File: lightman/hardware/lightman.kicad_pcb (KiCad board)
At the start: 2 copper layers, 139 x 80 mm, 39 parts, among them J1 DE15_Socket_HighDensity_Mount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, J2 Mini-DIN-6, J4 DE9_Pins, J5 Barrel_Jack_Switch, SW23 POWER, U1 MAX3232, U2 L7805, U3 MAX3232

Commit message: lightman pcb
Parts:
- added C13: 100n, IMNOTWOPR:C_Rect_P200mil, F.Cu at (71.8, 93.1)
- added C14: 100n, IMNOTWOPR:C_Rect_P200mil, F.Cu at (71.8, 100.7)
- added C15: 100n, IMNOTWOPR:C_Rect_P200mil, F.Cu at (69.3, 105.8)
- added C16: 100n, IMNOTWOPR:C_Rect_P200mil, F.Cu at (69.3, 95.6)
- added C17: 100n, IMNOTWOPR:C_Rect_P200mil, F.Cu at (80.7, 86.7)
- added F1: Polyfuse, Fuse:Fuse_Bourns_MF-RG700, F.Cu at (94.7, 60.0)
- added U5: MAX3232, IMNOTWOPR:DIP-16N, F.Cu at (79.5, 99.4)
- D3: footprint LED_THT:LED_D5.0mm -> LED_THT:LED_D5.0mm_Horizontal_O1.27mm_Z3.0mm
- R21: value 470 -> 1k
- U4: value ~ -> LEVEL SHIFTER
- moved A1 110.3 mm to (90.9, 88.0), turned to 0 degrees
- moved U4 96.5 mm to (76.9, 128.7), turned to 90 degrees
- moved J1 84.3 mm to (121.1, 148.1), turned to 0 degrees
- moved R4 67.2 mm to (130.3, 135.0), turned to -90 degrees
- moved J4 66.7 mm to (122.3, 54.4)
- moved U1 61.2 mm to (122.6, 62.6)
- moved R5 60.6 mm to (125.3, 135.0), turned to -90 degrees
- moved U3 60.6 mm to (122.6, 80.4)
- moved J2 55.8 mm to (88.1, 152.7)
- moved R6 54.2 mm to (120.3, 135.0), turned to -90 degrees
- moved R7 47.9 mm to (115.3, 135.0), turned to -90 degrees
- moved R8 45.8 mm to (130.1, 118.5), turned to -90 degrees
- moved R21 42.8 mm to (74.4, 151.5), turned to -90 degrees
- moved D3 41.6 mm to (68.2, 157.0)
- moved R9 40.0 mm to (125.3, 118.5), turned to -90 degrees
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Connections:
- A1 pad 10: /KEY_DATA_LO -> /PICO_RI
- A1 pad 11: unconnected-(A1-GPIO8-Pad11) -> /KEY_CLOCK_LO
- A1 pad 12: unconnected-(A1-GPIO9-Pad12) -> /KEY_DATA_LO
- A1 pad 9: /KEY_CLOCK_LO -> /PICO_DCD
- J4 pad 9: unconnected-(J4-Pad9) -> /RI
- J5 pad 1: Net-(D2-A) -> Net-(F1-Pad1)
- R21 pad 1: +9V -> +5V
- U3 pad 12: unconnected-(U3-R1OUT-Pad12) -> /PICO_DSR
- U3 pad 13: /DCD -> /DSR
- U3 pad 7: /RTR -> unconnected-(U3-T2OUT-Pad7)
- U3 pad 8: /DSR -> unconnected-(U3-R2IN-Pad8)
- U3 pad 9: /PICO_DSR -> unconnected-(U3-R2OUT-Pad9)
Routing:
- net GND: track 0.00 -> 457.9 mm
- net +5V: track 0.00 -> 122.8 mm
- net +3V3: track 0.00 -> 121.2 mm
- net /RI: track 0.00 -> 78.2 mm
- net /DCD: track 0.00 -> 70.0 mm
- net /BLUE: track 0.00 -> 56.1 mm
- net Net-(A1-GPIO20): track 0.00 -> 48.0 mm
- net +9V: track 0.00 -> 41.9 mm
- net /GREEN: track 0.00 -> 38.7 mm
- net /PICO_DSR: track 0.00 -> 38.6 mm
- net /PICO_DTR: track 0.00 -> 37.3 mm
- net /PICO_RTS: track 0.00 -> 36.0 mm
- net /PICO_CTS: track 0.00 -> 34.8 mm
- net /CTS: track 0.00 -> 33.0 mm
- net Net-(A1-GPIO19): track 0.00 -> 31.6 mm
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- added copper zone on B.Cu, net GND
- added copper zone on F.Cu, net GND
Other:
- board size 139 x 80 mm -> 74 x 119 mm
- board text added: "${COMPANY}"

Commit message: lightman pcb
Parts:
- removed R12, R13, R14, R15: 1k, IMNOTWOPR:R_Axial_DIN0207_P400mil
- C1: renamed from C31; footprint Desval27:C_Disc_D5.0mm_W2.5mm_P200mil -> IMNOTWOPR:C_Rect_P200mil
- C4: renamed from C30; footprint Desval27:C_Disc_D5.0mm_W2.5mm_P200mil -> IMNOTWOPR:C_Rect_P200mil
- R1: renamed from R21; footprint Desval27:R_Axial_DIN0207_400mil -> IMNOTWOPR:R_Axial_DIN0207_P400mil
- R2: renamed from R4; value 1k -> 470R
- R4: renamed from R6; value 1k -> 2k2
- R5: renamed from R7; value 1k -> 470R
- R7: renamed from R9; value 1k -> 2k2
- R8: renamed from R10; value 1k -> 390R
- moved C13 59.8 mm to (129.0, 109.6), turned to 0 degrees
- moved C10 52.5 mm to (123.9, 107.1), turned to 0 degrees
- moved C16 51.5 mm to (118.8, 109.6), turned to 0 degrees
- moved C7 46.6 mm to (116.3, 107.1), turned to 0 degrees
- moved U5 43.2 mm to (122.6, 99.5), turned to 90 degrees
- moved C19 31.4 mm to (109.9, 98.2), turned to -90 degrees
- moved R6 10.7 mm to (122.6, 126.1), turned to 0 degrees
- moved R5 8.96 mm to (122.6, 129.9), turned to 0 degrees
- moved R2 8.13 mm to (125.2, 141.4), turned to 0 degrees
- moved A1 6.35 mm to (87.1, 93.1)
- moved R9 6.16 mm to (120.1, 114.7), turned to 0 degrees
- moved R4 5.08 mm to (125.2, 133.7), turned to 0 degrees
- moved R7 4.62 mm to (122.6, 122.3), turned to 0 degrees
- moved U1 2.84 mm to (75.7, 131.2)
- moved R3 2.54 mm to (125.2, 137.6), turned to 0 degrees
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- renumbered C14 to C10, C6 to C11, C10 to C12, C15 to C13, C5 to C14, C11 to C15, C7 to C17, C12 to C18, C17 to C19, C1 to C2, C2 to C3, C3 to C5, C8 to C6, C13 to C7, C4 to C8, D2 to D1, D3 to D2, J5 to J1, J1 to J3, R5 to R3, R8 to R6, R11 to R9, SW23 to SW1, U4 to U1, U1 to U3, U3 to U4
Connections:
- A1 pad 1: /PICO_TXD -> /PICO_RXD
- A1 pad 17: unconnected-(A1-GPIO13-Pad17) -> /HSYNC
- A1 pad 19: unconnected-(A1-GPIO14-Pad19) -> /VSYNC
- A1 pad 2: /PICO_RXD -> /PICO_TXD
- A1 pad 20: unconnected-(A1-GPIO15-Pad20) -> /R0
- A1 pad 21: /HSYNC -> /R1
- A1 pad 22: /VSYNC -> /R2
- A1 pad 24: Net-(A1-GPIO18) -> /G0
- A1 pad 25: Net-(A1-GPIO19) -> /G1
- A1 pad 26: Net-(A1-GPIO20) -> /G2
- A1 pad 27: unconnected-(A1-GPIO21-Pad27) -> /B0
- A1 pad 29: unconnected-(A1-GPIO22-Pad29) -> /B1
- A1 pad 4: /PICO_CTS -> /PICO_RTS
- A1 pad 5: /PICO_RTS -> /PICO_CTS
- A1 pad 6: /PICO_DTR -> /PICO_DSR
- A1 pad 7: /PICO_DSR -> /PICO_DTR
- R2 pad 1: Net-(A1-GPIO18) -> /R0
- R3 pad 1: Net-(A1-GPIO18) -> /R1
- R4 pad 1: Net-(A1-GPIO18) -> /R2
- R5 pad 1: Net-(A1-GPIO18) -> /G0
- R5 pad 2: /RED -> /GREEN
- R6 pad 1: Net-(A1-GPIO19) -> /G1
- R7 pad 1: Net-(A1-GPIO19) -> /G2
- R8 pad 1: Net-(A1-GPIO19) -> /B0
- R8 pad 2: /GREEN -> /BLUE
- R9 pad 1: Net-(A1-GPIO19) -> /B1
- R9 pad 2: /GREEN -> /BLUE
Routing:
- net GND: track 457.9 -> 191.5 mm
- net /PICO_RI: track 8.74 -> 64.8 mm
- net /PICO_CTS: track 34.8 -> 88.9 mm
- net /R0: track 0.00 -> 49.9 mm
- net Net-(A1-GPIO20): track 48.0 -> 0.00 mm
- net /PICO_RTS: track 36.0 -> 83.8 mm
- net /PICO_TXD: track 29.7 -> 76.2 mm
- net /PICO_DCD: track 12.4 -> 56.4 mm
- net /PICO_RXD: track 31.0 -> 71.1 mm
- net /DSR: track 0.00 -> 38.9 mm
- net /PICO_DTR: track 37.3 -> 70.5 mm
- net Net-(A1-GPIO19): track 31.6 -> 0.00 mm
- net /PICO_DSR: track 38.6 -> 65.4 mm
- net /DCD: track 70.0 -> 46.1 mm, vias 0 -> 1
- net Net-(A1-GPIO18): track 21.6 -> 0.00 mm
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
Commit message: routing-first-stage
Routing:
- net +3V3: track 114.6 -> 0.00 mm, vias 1 -> 0
- net +5V: track 129.3 -> 16.6 mm
- net GND: track 191.5 -> 94.8 mm, vias 0 -> 8
- net /PICO_CTS: track 88.9 -> 0.00 mm
- net /PICO_RTS: track 83.8 -> 0.00 mm
- net /PICO_TXD: track 76.2 -> 0.00 mm
- net /PICO_RXD: track 71.1 -> 0.00 mm
- net /PICO_DTR: track 70.5 -> 0.00 mm
- net /PICO_DSR: track 65.4 -> 0.00 mm
- net /PICO_RI: track 64.8 -> 0.00 mm
- net /RI: track 60.2 -> 0.00 mm
- net /PICO_DCD: track 56.4 -> 0.00 mm
- net /R0: track 49.9 -> 0.00 mm
- net /HSYNC: track 48.4 -> 0.00 mm
- net /DCD: track 46.1 -> 0.00 mm, vias 1 -> 0
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
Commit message: numerous updates; documentation, ferruous, lightman, etc.
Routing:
- net GND: track 94.8 -> 536.3 mm
- net +3V3: track 0.00 -> 112.1 mm
- net +5V: track 16.6 -> 119.3 mm
- net /RI: track 0.00 -> 70.8 mm
- net /HSYNC: track 0.00 -> 48.6 mm
- net /VSYNC: track 0.00 -> 38.4 mm
- net /BLUE: track 0.00 -> 37.5 mm
- net /R0: track 0.00 -> 33.3 mm
- net /GREEN: track 0.00 -> 30.0 mm
- net /RTS: track 0.00 -> 29.4 mm
- net /CTS: track 0.00 -> 24.6 mm
- net /RED: track 0.00 -> 22.8 mm
- net /KEY_DATA_HI: track 0.00 -> 18.5 mm
- net /KEY_CLOCK_HI: track 0.00 -> 18.0 mm
- net /R2: track 0.00 -> 16.1 mm
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
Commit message: tracework for lightman
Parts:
- moved C1 2.54 mm to (70.6, 71.5)
- moved C3 2.54 mm to (89.6, 67.7)
- moved U2 2.54 mm to (78.2, 81.7)
- moved C2 2.54 mm to (69.3, 65.2)
- moved D1 2.54 mm to (68.0, 57.5)
- moved F1 2.54 mm to (94.7, 62.5)
- moved J1 2.54 mm to (91.9, 56.9)
- moved C4 2.54 mm to (90.9, 74.0)
- moved SW1 1.27 mm to (77.7, 49.3)
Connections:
- A1 pad 1: /PICO_RXD -> /PICO_TXD
- A1 pad 2: /PICO_TXD -> /PICO_RXD
- A1 pad 4: /PICO_RTS -> /PICO_CTS
- A1 pad 5: /PICO_CTS -> /PICO_RTS
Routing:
- net /PICO_CTS: track 0.00 -> 77.2 mm
- net /PICO_RTS: track 0.00 -> 73.0 mm
- net /PICO_TXD: track 0.00 -> 64.6 mm
- net /PICO_RXD: track 0.00 -> 61.4 mm
- net /DCD: track 0.00 -> 56.5 mm
- net /PICO_DTR: track 0.00 -> 55.6 mm
- net /PICO_RI: track 0.00 -> 52.9 mm
- net /PICO_DSR: track 0.00 -> 51.6 mm
- net /DSR: track 0.00 -> 44.7 mm
- net /PICO_DCD: track 0.00 -> 44.2 mm
- net /DTR: track 0.00 -> 24.8 mm
- net GND: track 536.3 -> 557.1 mm, vias 8 -> 0
- net /CTS: track 24.6 -> 37.8 mm
- net /RTS: track 29.4 -> 18.8 mm
- net +5V: track 119.3 -> 114.6 mm
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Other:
- board text added: "${COMMENT3}"
- board text added: "${COMPANY} - ${COMMENT1} ${TITLE} | ${COMMENT4} | ${COMMENT2} REVISION ${REVISION} ${CURRENT_DATE}"
- board text removed: "${COMPANY}"

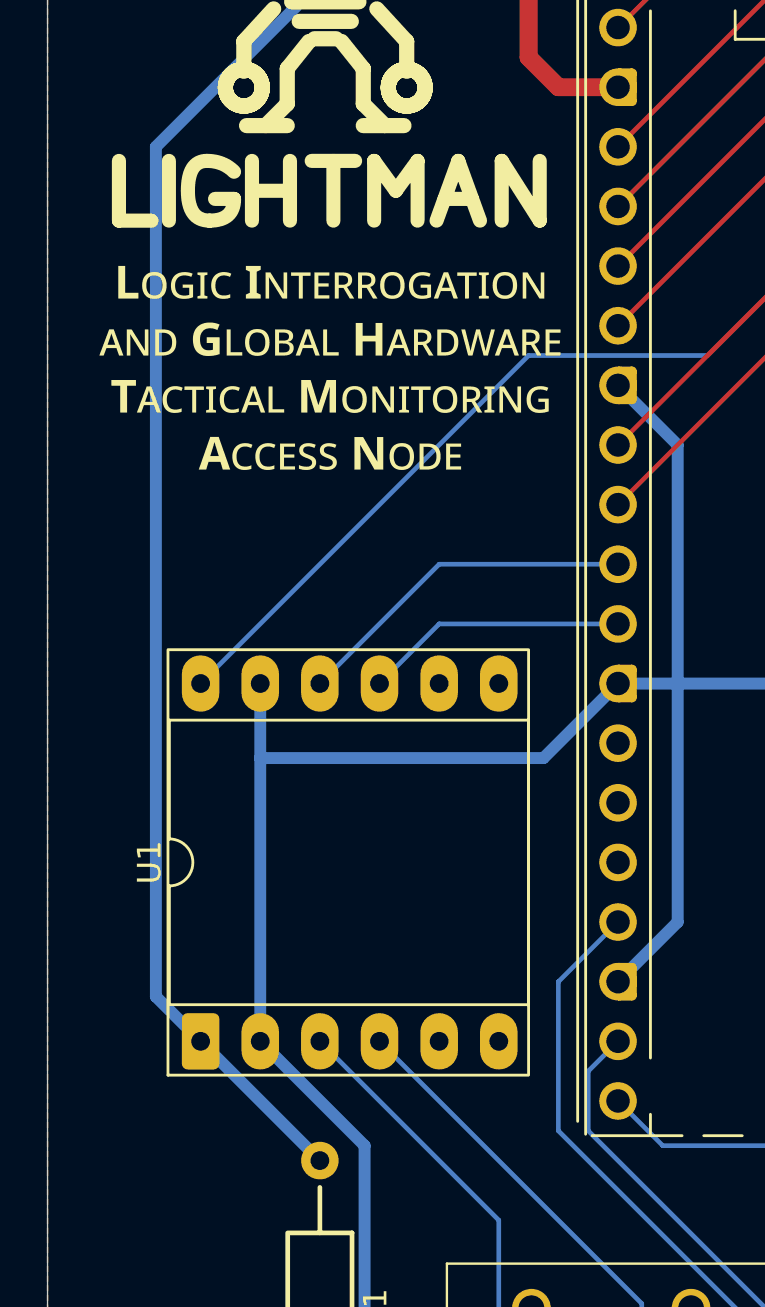
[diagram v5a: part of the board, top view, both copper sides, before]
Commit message: fixed level shifter footprint width
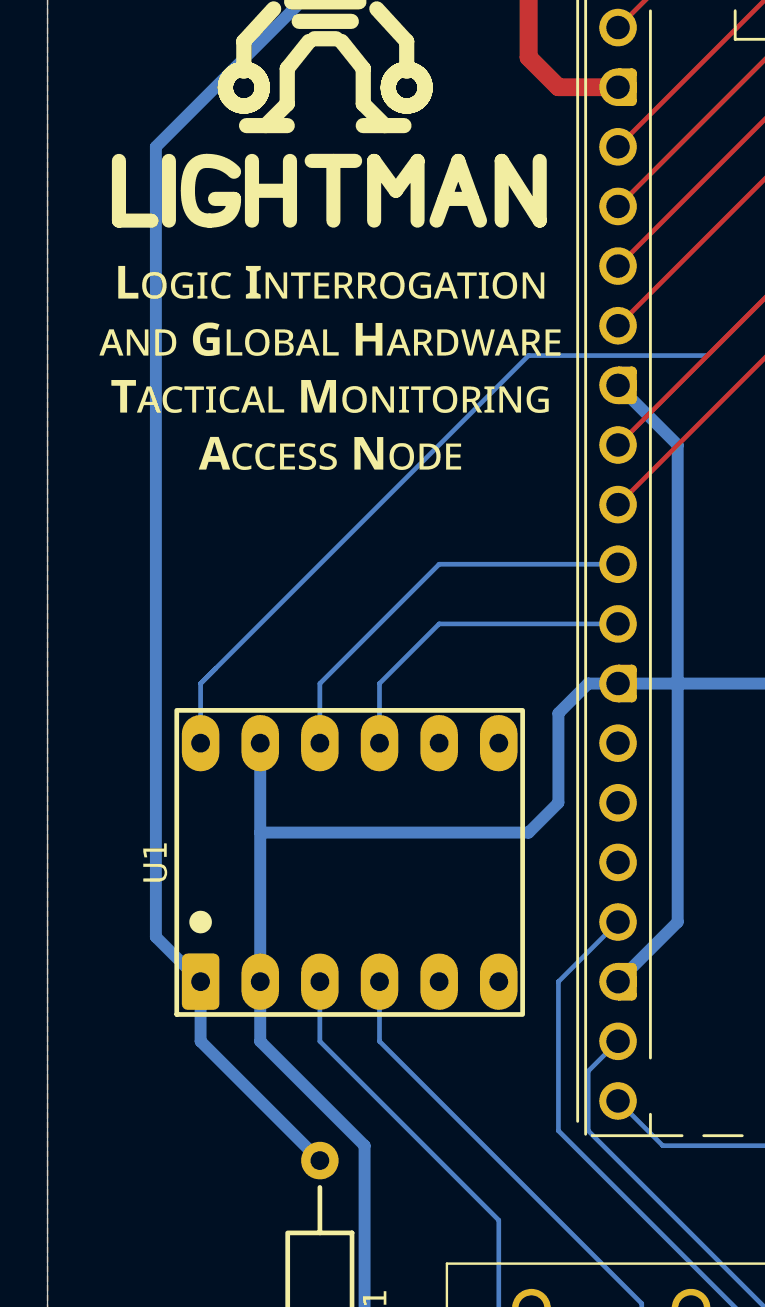
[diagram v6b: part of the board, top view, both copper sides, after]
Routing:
- net +3V3: track 110.2 -> 113.6 mm
- net /KEY_DATA_LO: track 11.2 -> 13.8 mm
- net /KEY_CLOCK_LO: track 14.8 -> 17.3 mm
- net /KEY_DATA_HI: track 18.5 -> 21.0 mm
- net /KEY_CLOCK_HI: track 17.6 -> 20.1 mm
- net GND: track 557.1 -> 558.1 mm

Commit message: lightman cleanup; more work pending
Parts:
- C2: footprint Capacitor_THT:CP_Radial_D6.3mm_P2.50mm -> Capacitor_THT:CP_Radial_D10.0mm_P5.00mm
- C3: footprint Capacitor_THT:CP_Radial_D5.0mm_P2.50mm -> Capacitor_THT:CP_Radial_D10.0mm_P5.00mm
- moved C3 21.9 mm to (72.7, 81.7)
- moved C4 21.9 mm to (75.2, 89.3)
- moved U2 7.41 mm to (84.5, 85.5)
- moved C1 5.51 mm to (75.2, 74.5)
- moved C2 3.90 mm to (72.7, 67.1)
- moved F1 2.66 mm to (92.2, 63.3)
- moved R1 2.57 mm to (76.9, 150.7)
- turned U1 to -90 degrees
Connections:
- U1 pad 1: +5V -> /KEY_DATA_LO
- U1 pad 10: /KEY_CLOCK_LO -> +5V
- U1 pad 11: GND -> /KEY_CLOCK_HI
- U1 pad 12: +3V3 -> /KEY_DATA_HI
- U1 pad 2: GND -> /KEY_CLOCK_LO
- U1 pad 3: /KEY_CLOCK_HI -> +3V3
- U1 pad 4: /KEY_DATA_HI -> GND
- U1 pad 9: /KEY_DATA_LO -> GND
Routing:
- net GND: track 558.1 -> 493.6 mm
- net +5V: track 114.6 -> 87.2 mm
- net +9V: track 43.6 -> 30.3 mm
- net Net-(D1-A): track 7.93 -> 0.00 mm
- net Net-(F1-Pad1): track 6.84 -> 0.00 mm
- net +3V3: track 113.6 -> 109.6 mm
- net /KEY_DATA_LO: track 13.8 -> 10.2 mm
- net Net-(D2-A): track 3.19 -> 6.14 mm
- net /KEY_DATA_HI: track 21.0 -> 18.9 mm
- net /KEY_CLOCK_HI: track 20.1 -> 18.0 mm
- net /KEY_CLOCK_LO: track 17.3 -> 15.2 mm
- net unconnected-(U1-LV3-Pad5): track 0.00 -> 0.63 mm

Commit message: lightman pcb gerbers
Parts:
- J4: footprint Connector_Dsub:DSUB-9_Pins_Horizontal_P2.77x2.54mm_EdgePinOffset9.40mm -> IMNOTWOPR:D-Sub 9 CNR Series
- moved J4 5.66 mm to (117.2, 52.0), turned to 0 degrees
- moved F1 0.24 mm to (91.9, 63.3)
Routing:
- net GND: track 493.6 -> 529.5 mm
- net +5V: track 87.2 -> 119.9 mm
- net +9V: track 30.3 -> 50.3 mm
- net Net-(D1-A): track 0.00 -> 6.92 mm
- net Net-(F1-Pad1): track 0.00 -> 6.38 mm
- net /DSR: track 44.7 -> 49.2 mm
- net /RTS: track 18.8 -> 20.7 mm
- net /TXD: track 5.23 -> 6.17 mm
- net /DTR: track 24.8 -> 25.6 mm
- net /RXD: track 5.13 -> 5.98 mm
- net /CTS: track 37.8 -> 38.6 mm
- net unconnected-(J2-Pad6): track 0.00 -> 0.58 mm
